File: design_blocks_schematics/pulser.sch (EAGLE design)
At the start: 52 parts

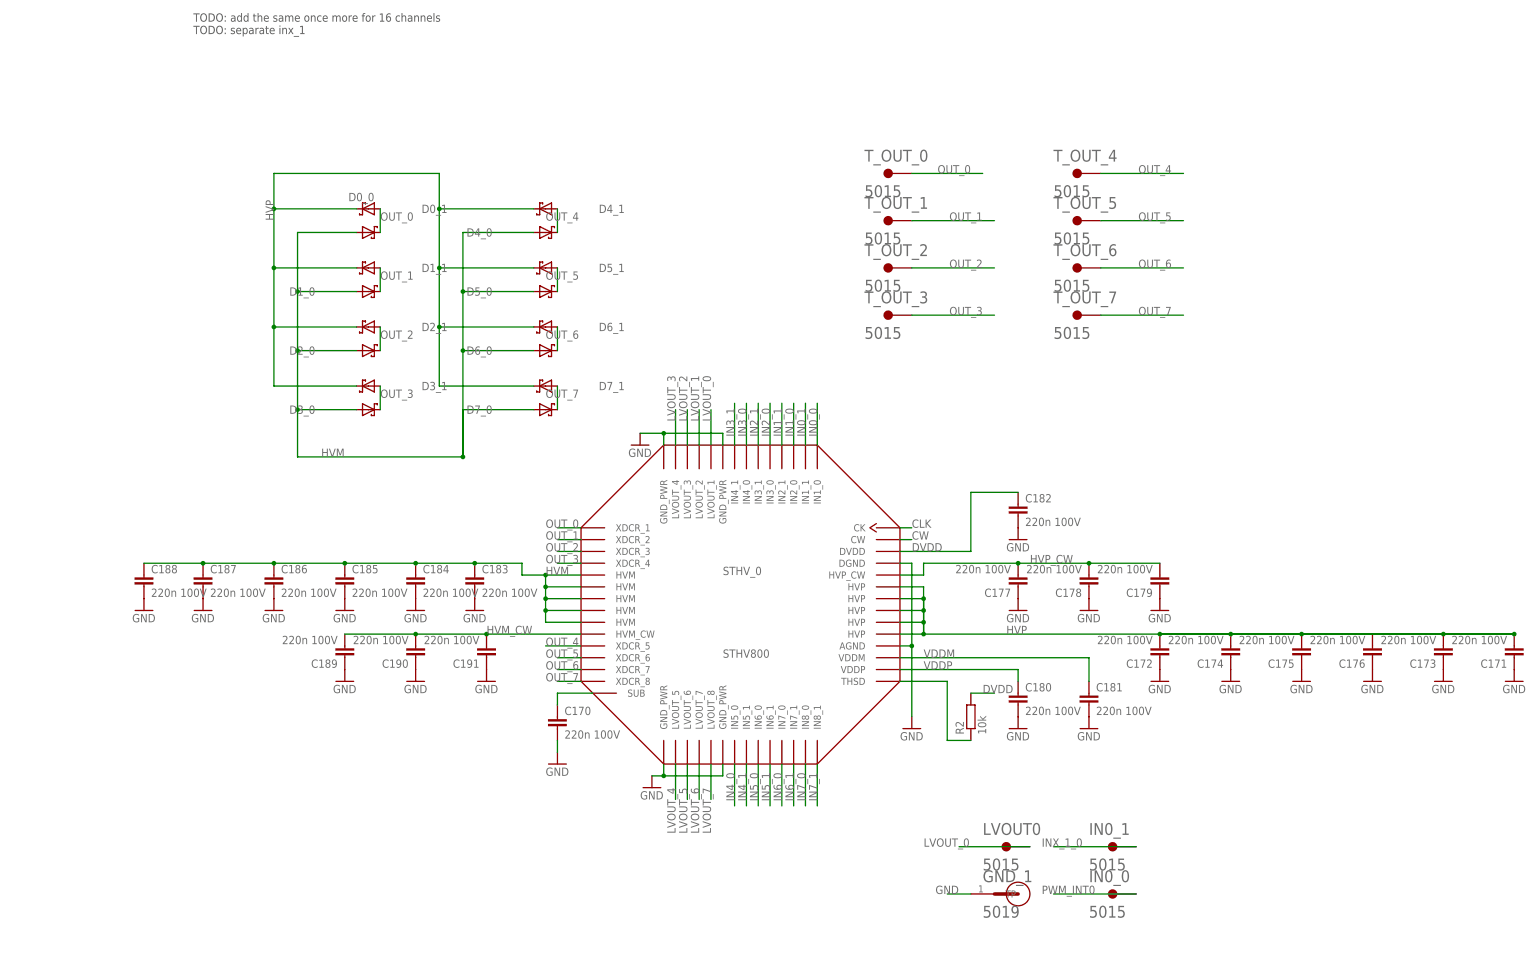
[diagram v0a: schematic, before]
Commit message: added design block for sthv800 pulser chip
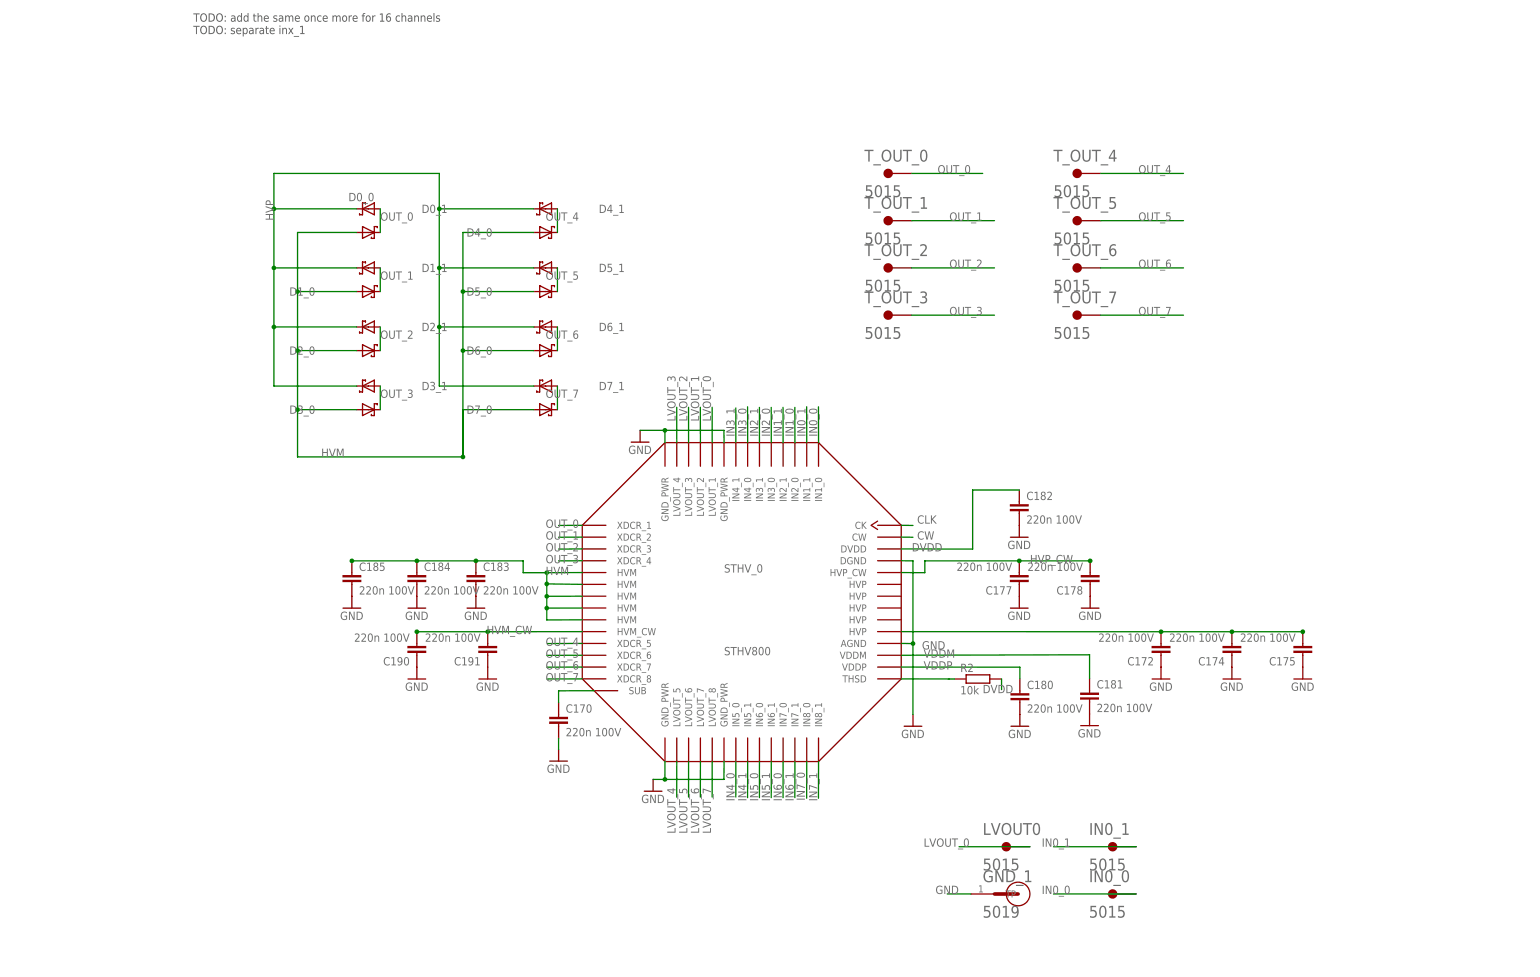
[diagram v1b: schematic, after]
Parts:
- removed C171, C173, C176, C179, C186, C187, C188, C189: 220n 100V, rcl:C-EUC0805
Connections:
- removed net INX_1_0: IN0_1.TP
- removed net PWM_INT0: IN0_0.TP
- net GND: no longer C171.1, C173.1, C176.1, C179.1, C186.2, C187.2, C188.2, C189.1
- net HVM: no longer C186.1, C187.1, C188.1
- net HVM_CW: no longer C189.2
- net HVP: no longer C171.2, C173.2, C176.2, STHV_0.HVP@1, STHV_0.HVP@2, STHV_0.HVP@3, STHV_0.HVP@4
- net HVP_CW: no longer C179.2
- net IN0_0: now also IN0_0.TP
- net IN0_1: now also IN0_1.TP
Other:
- moved on the sheet: C170, C172, C174, C175, C177, C178, C180, C181, C182, C183, C184, C185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

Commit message: cleaned up schematic of sthv_800
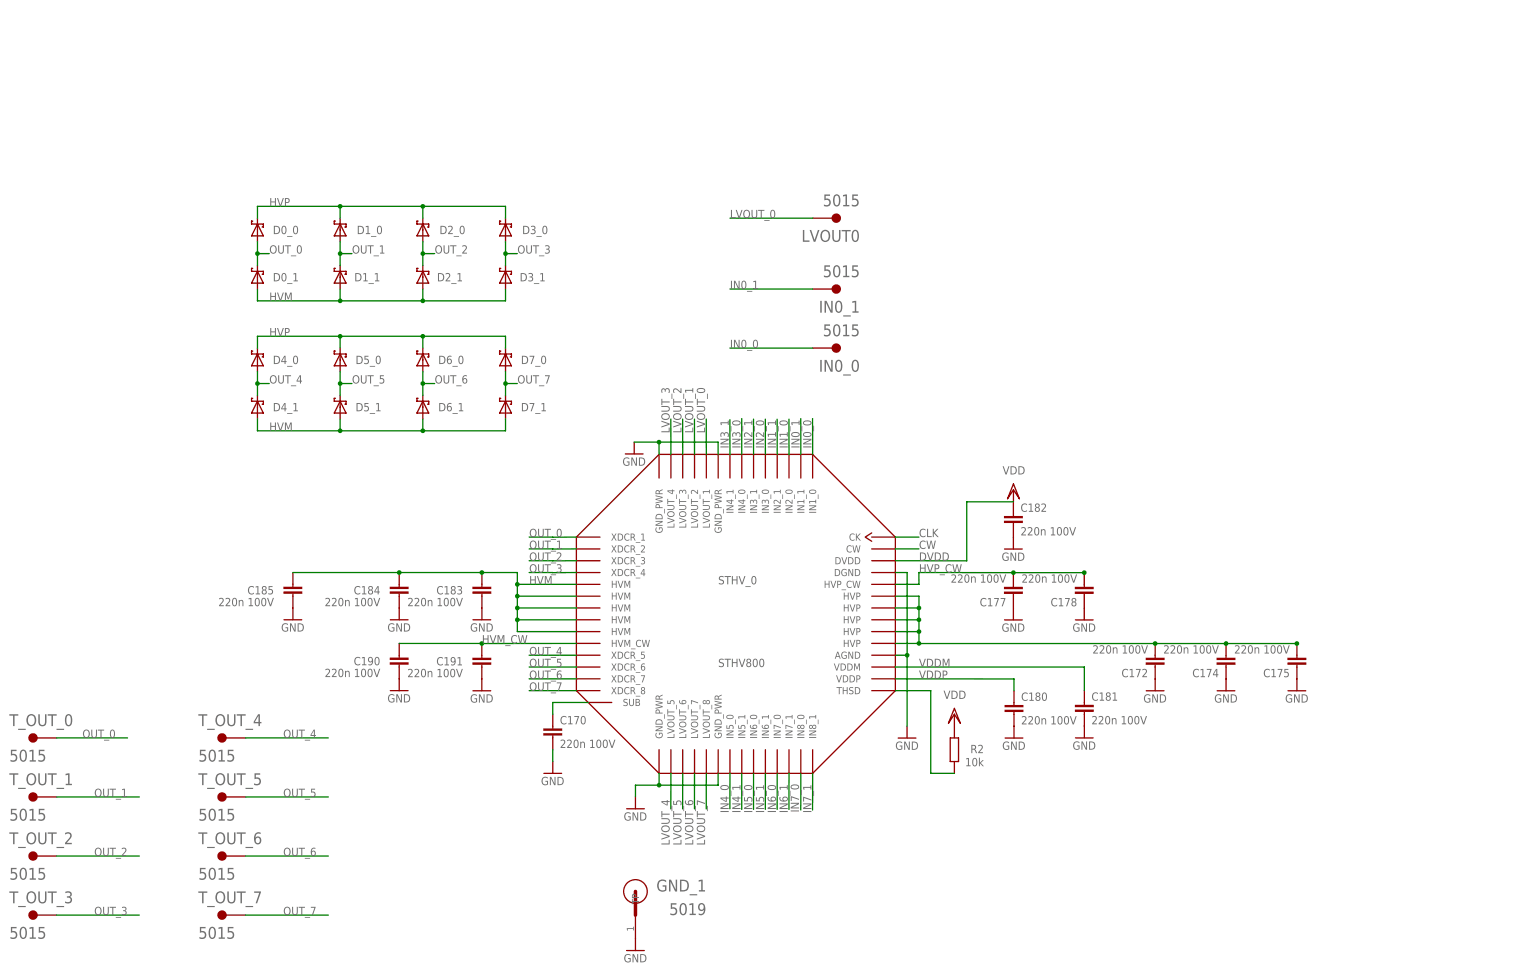
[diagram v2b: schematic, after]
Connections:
- new net VDD: R2.2
- net DVDD: no longer R2.2
- net HVP: now also STHV_0.HVP@1, STHV_0.HVP@2, STHV_0.HVP@3, STHV_0.HVP@4
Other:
- note removed: "TODO: add the same once more for 16 channels TODO: separate inx_1"
- note removed: "boost circuit 0-7"
- moved on the sheet: C170, C172, C174, C175, C177, C178, C180, C181, C182, C183, C184, C185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

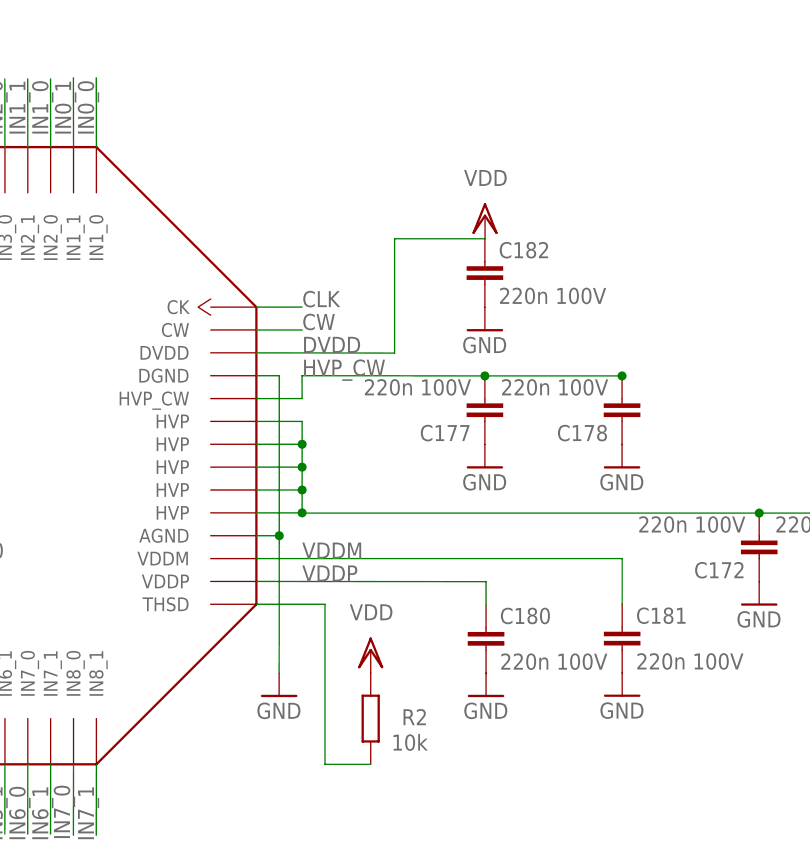
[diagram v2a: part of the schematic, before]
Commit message: sthv800 update: connected dvdd & vddp
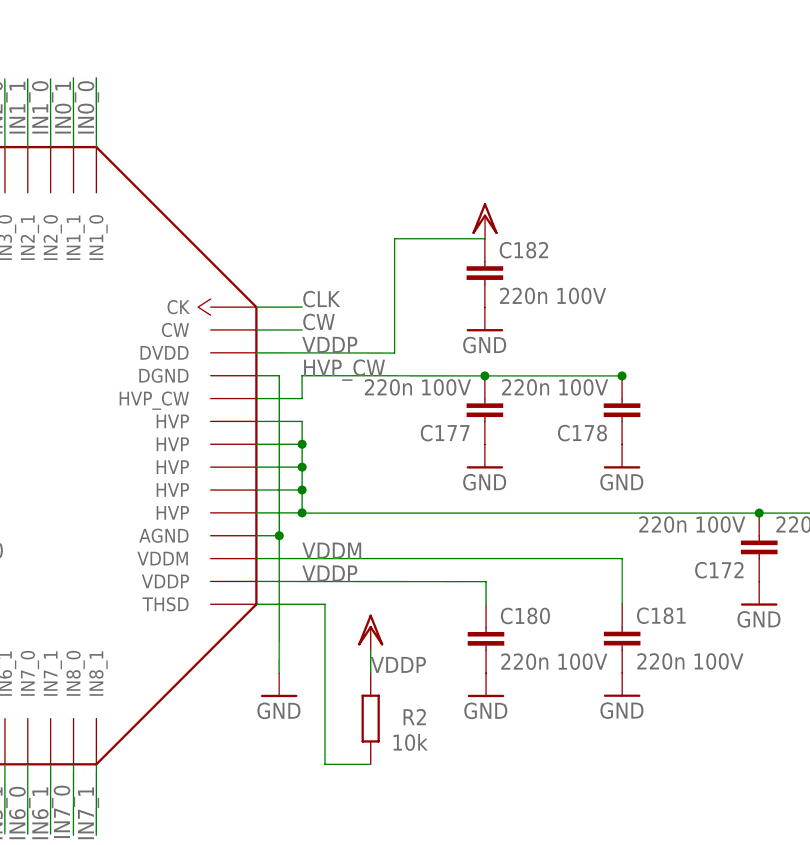
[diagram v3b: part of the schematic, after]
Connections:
- removed net DVDD: C182.1, STHV_0.DVDD
- removed net VDD: R2.2
- net VDDP: now also C182.1, R2.2, STHV_0.DVDD
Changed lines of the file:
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@@
 <?xml version="1.0" encoding="utf-8"?>
 <!DOCTYPE eagle SYSTEM "eagle.dtd">
-<eagle version="9.5.0">
+<eagle version="9.5.1">
 <drawing>
 <settings>
@@
 <part name="GND25" library="supply1" library_urn="urn:adsk.eagle:library:371" deviceset="GND" device=""/>
 <part name="GND4" library="supply1" library_urn="urn:adsk.eagle:library:371" deviceset="GND" device=""/>
-<part name="VDD1" library="supply1" library_urn="urn:adsk.eagle:library:371" deviceset="VDD" device=""/>
-<part name="VDD2" library="supply1" library_urn="urn:adsk.eagle:library:371" deviceset="VDD" device=""/>
+<part name="VDDP1" library="supply1" library_urn="urn:adsk.eagle:library:371" deviceset="VDD" device=""/>
+<part name="VDDP2" library="supply1" library_urn="urn:adsk.eagle:library:371" deviceset="VDD" device=""/>
 </parts>
 <sheets>
@@
 <attribute name="VALUE" x="149.86" y="45.72" size="1.778" layer="96"/>
 </instance>
-<instance part="VDD1" gate="G$1" x="233.68" y="147.32" smashed="yes">
-<attribute name="VALUE" x="236.22" y="152.4" size="1.778" layer="96" rot="R180"/>
-</instance>
-<instance part="VDD2" gate="G$1" x="220.98" y="99.06" smashed="yes">
-<attribute name="VALUE" x="223.52" y="104.14" size="1.778" layer="96" rot="R180"/>
-</instance>
+<instance part="VDDP1" gate="G$1" x="233.68" y="147.32" smashed="yes"/>
+<instance part="VDDP2" gate="G$1" x="220.98" y="101.6" smashed="yes"/>
 </instances>
 <busses>
@@
 <wire x1="233.7943" y1="106.6546" x2="208.28" y2="106.68" width="0.1524" layer="91"/>
 </segment>
+<segment>
+<pinref part="R2" gate="G$1" pin="2"/>
+<pinref part="VDDP2" gate="G$1" pin="VDD"/>
+<wire x1="220.98" y1="99.06" x2="220.98" y2="96.52" width="0.1524" layer="91"/>
+<label x="220.98" y="96.52" size="1.778" layer="95"/>
+</segment>
+<segment>
+<pinref part="STHV_0" gate="G$1" pin="DVDD"/>
+<label x="213.36" y="132.08" size="1.778" layer="95"/>
+<pinref part="C182" gate="G$1" pin="1"/>
+<wire x1="208.28" y1="132.08" x2="223.6343" y2="132.0546" width="0.1524" layer="91"/>
+<wire x1="223.6343" y1="132.0546" x2="223.6343" y2="144.7546" width="0.1524" layer="91"/>
+<wire x1="223.6343" y1="144.7546" x2="233.6673" y2="144.7546" width="0.1524" layer="91"/>
+</segment>
 </net>
 <net name="VDDM" class="1">
@@
 <wire x1="167.64" y1="86.36" x2="167.6273" y2="78.7146" width="0.1524" layer="91"/>
 <label x="167.3733" y="80.7466" size="1.778" layer="95" rot="R270" align="top-left"/>
-</segment>
-</net>
-<net name="DVDD" class="0">
-<segment>
-<pinref part="STHV_0" gate="G$1" pin="DVDD"/>
-<label x="213.36" y="132.08" size="1.778" layer="95"/>
-<pinref part="C182" gate="G$1" pin="1"/>
-<wire x1="208.28" y1="132.08" x2="223.6343" y2="132.0546" width="0.1524" layer="91"/>
-<wire x1="223.6343" y1="132.0546" x2="223.6343" y2="144.7546" width="0.1524" layer="91"/>
-<wire x1="223.6343" y1="144.7546" x2="233.6673" y2="144.7546" width="0.1524" layer="91"/>
 </segment>
 </net>
@@
 </segment>
 </net>
-<net name="VDD" class="0">
-<segment>
-<pinref part="R2" gate="G$1" pin="2"/>
-<pinref part="VDD2" gate="G$1" pin="VDD"/>
-</segment>
-</net>

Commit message: missing .sch from previous commit
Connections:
- new net DVDD: C182.1, STHV_0.DVDD
- new net VDD: R2.2
- net VDDP: no longer C182.1, R2.2, STHV_0.DVDD
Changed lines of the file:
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@@
 <?xml version="1.0" encoding="utf-8"?>
 <!DOCTYPE eagle SYSTEM "eagle.dtd">
-<eagle version="9.5.1">
+<eagle version="9.5.0">
 <drawing>
 <settings>
@@
 <part name="GND25" library="supply1" library_urn="urn:adsk.eagle:library:371" deviceset="GND" device=""/>
 <part name="GND4" library="supply1" library_urn="urn:adsk.eagle:library:371" deviceset="GND" device=""/>
-<part name="VDDP1" library="supply1" library_urn="urn:adsk.eagle:library:371" deviceset="VDD" device=""/>
-<part name="VDDP2" library="supply1" library_urn="urn:adsk.eagle:library:371" deviceset="VDD" device=""/>
+<part name="VDD1" library="supply1" library_urn="urn:adsk.eagle:library:371" deviceset="VDD" device=""/>
+<part name="VDD2" library="supply1" library_urn="urn:adsk.eagle:library:371" deviceset="VDD" device=""/>
 </parts>
 <sheets>
@@
 <attribute name="VALUE" x="208.2673" y="91.4146" size="1.778" layer="96"/>
 </instance>
-<instance part="GND2" gate="1" x="152.1333" y="155.0416" smashed="yes">
-<attribute name="VALUE" x="149.5933" y="152.5016" size="1.778" layer="96"/>
+<instance part="GND2" gate="1" x="149.86" y="154.94" smashed="yes">
+<attribute name="VALUE" x="147.32" y="152.4" size="1.778" layer="96"/>
 </instance>
 <instance part="GND3" gate="1" x="152.4" y="78.74" smashed="yes">
@@
 <attribute name="VALUE" x="149.86" y="45.72" size="1.778" layer="96"/>
 </instance>
-<instance part="VDDP1" gate="G$1" x="233.68" y="147.32" smashed="yes"/>
-<instance part="VDDP2" gate="G$1" x="220.98" y="101.6" smashed="yes"/>
+<instance part="VDD1" gate="G$1" x="233.68" y="147.32" smashed="yes">
+<attribute name="VALUE" x="236.22" y="152.4" size="1.778" layer="96" rot="R180"/>
+</instance>
+<instance part="VDD2" gate="G$1" x="220.98" y="99.06" smashed="yes">
+<attribute name="VALUE" x="223.52" y="104.14" size="1.778" layer="96" rot="R180"/>
+</instance>
 </instances>
 <busses>
@@
 <segment>
 <pinref part="STHV_0" gate="G$1" pin="GND_PWR@4"/>
-<wire x1="157.48" y1="154.94" x2="157.4673" y2="157.5816" width="0.1524" layer="91"/>
+<wire x1="157.48" y1="154.94" x2="157.48" y2="157.48" width="0.1524" layer="91"/>
 <pinref part="GND2" gate="1" pin="GND"/>
-<wire x1="152.1333" y1="157.5816" x2="157.4673" y2="157.5816" width="0.1524" layer="91"/>
+<wire x1="149.86" y1="157.48" x2="157.48" y2="157.48" width="0.1524" layer="91"/>
 <pinref part="STHV_0" gate="G$1" pin="GND_PWR@3"/>
-<wire x1="170.18" y1="154.94" x2="170.1673" y2="157.5816" width="0.1524" layer="91"/>
-<wire x1="157.4673" y1="157.5816" x2="170.1673" y2="157.5816" width="0.1524" layer="91"/>
-<junction x="157.4673" y="157.5816"/>
+<wire x1="170.18" y1="154.94" x2="170.18" y2="157.48" width="0.1524" layer="91"/>
+<wire x1="157.48" y1="157.48" x2="170.18" y2="157.48" width="0.1524" layer="91"/>
+<junction x="157.48" y="157.48"/>
 </segment>
 <segment>
@@
 <wire x1="233.7943" y1="106.6546" x2="208.28" y2="106.68" width="0.1524" layer="91"/>
 </segment>
-<segment>
-<pinref part="R2" gate="G$1" pin="2"/>
-<pinref part="VDDP2" gate="G$1" pin="VDD"/>
-<wire x1="220.98" y1="99.06" x2="220.98" y2="96.52" width="0.1524" layer="91"/>
-<label x="220.98" y="96.52" size="1.778" layer="95"/>
-</segment>
-<segment>
-<pinref part="STHV_0" gate="G$1" pin="DVDD"/>
-<label x="213.36" y="132.08" size="1.778" layer="95"/>
-<pinref part="C182" gate="G$1" pin="1"/>
-<wire x1="208.28" y1="132.08" x2="223.6343" y2="132.0546" width="0.1524" layer="91"/>
-<wire x1="223.6343" y1="132.0546" x2="223.6343" y2="144.7546" width="0.1524" layer="91"/>
-<wire x1="223.6343" y1="144.7546" x2="233.6673" y2="144.7546" width="0.1524" layer="91"/>
-</segment>
 </net>
 <net name="VDDM" class="1">
@@
 <wire x1="167.64" y1="86.36" x2="167.6273" y2="78.7146" width="0.1524" layer="91"/>
 <label x="167.3733" y="80.7466" size="1.778" layer="95" rot="R270" align="top-left"/>
+</segment>
+</net>
+<net name="DVDD" class="0">
+<segment>
+<pinref part="STHV_0" gate="G$1" pin="DVDD"/>
+<label x="213.36" y="132.08" size="1.778" layer="95"/>
+<pinref part="C182" gate="G$1" pin="1"/>
+<wire x1="208.28" y1="132.08" x2="223.6343" y2="132.0546" width="0.1524" layer="91"/>
+<wire x1="223.6343" y1="132.0546" x2="223.6343" y2="144.7546" width="0.1524" layer="91"/>
+<wire x1="223.6343" y1="144.7546" x2="233.6673" y2="144.7546" width="0.1524" layer="91"/>
 </segment>
 </net>
@@
 </segment>
 </net>
+<net name="VDD" class="0">
+<segment>
+<pinref part="R2" gate="G$1" pin="2"/>
+<pinref part="VDD2" gate="G$1" pin="VDD"/>
+</segment>
+</net>
